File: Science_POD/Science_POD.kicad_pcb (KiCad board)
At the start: 2 copper layers, 24.6 x 59.9 mm, 10 parts, among them U1 Molex_SL_2, U2 AP1059, U3 ESP_8266_Breakout_Small, U4 Molex_SL_3, U5 Molex_SL_2

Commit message: finalised board
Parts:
- added G***: LOGO, MRDT_Silkscreens:Andrew_Van_Horn_Sig_15mm, B.Cu at (190.6, 106.8)
- added G***: LOGO, MRDT_Silkscreens:MRDT_Logo_10mm, B.Cu at (180.9, 110.9)
- added R2: 10K, Resistors_SMD:R_0603_HandSoldering, F.Cu at (176.0, 119.1)
- R1: value 100 -> 10K
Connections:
- U3 pad 7: /Ain -> Net-(R2-Pad2)
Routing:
- net /Ain: track 33.9 -> 30.3 mm
- net Net-(R2-Pad2): track 0.00 -> 3.13 mm
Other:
- board size 24.6 x 59.9 mm -> 25.9 x 59.9 mm
- board text added: "Moisture"
- board text added: "Sensor Pod, Rev 1 MRDT 2018 Missouri S&T Andrew Van Horn"
- board text added: "Temperature"

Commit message: Generated Final Gerbs
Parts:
- added D2: LED, Diodes_SMD:D_1206, F.Cu at (170.8, 93.4)
- added R3: 330, Resistors_SMD:R_0603_HandSoldering, F.Cu at (170.8, 98.3)
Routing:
- net /+3V3: track 36.6 -> 41.4 mm
- net Net-(D2-Pad2): track 0.00 -> 2.29 mm
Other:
- board size 25.9 x 59.9 mm -> 38.1 x 59.9 mm
- board text added: "Power"

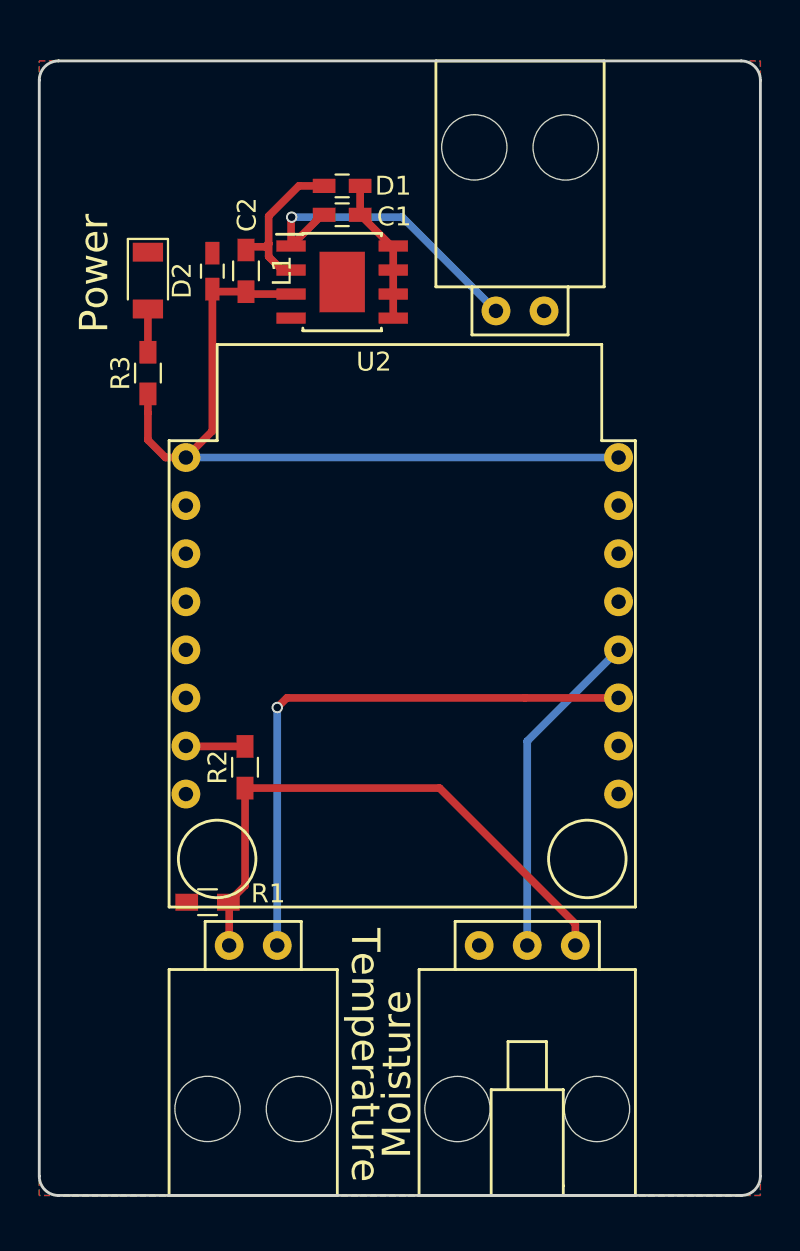
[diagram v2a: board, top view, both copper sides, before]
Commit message: Rev 2-added SL-3 for thermister. Fixed esp footprint
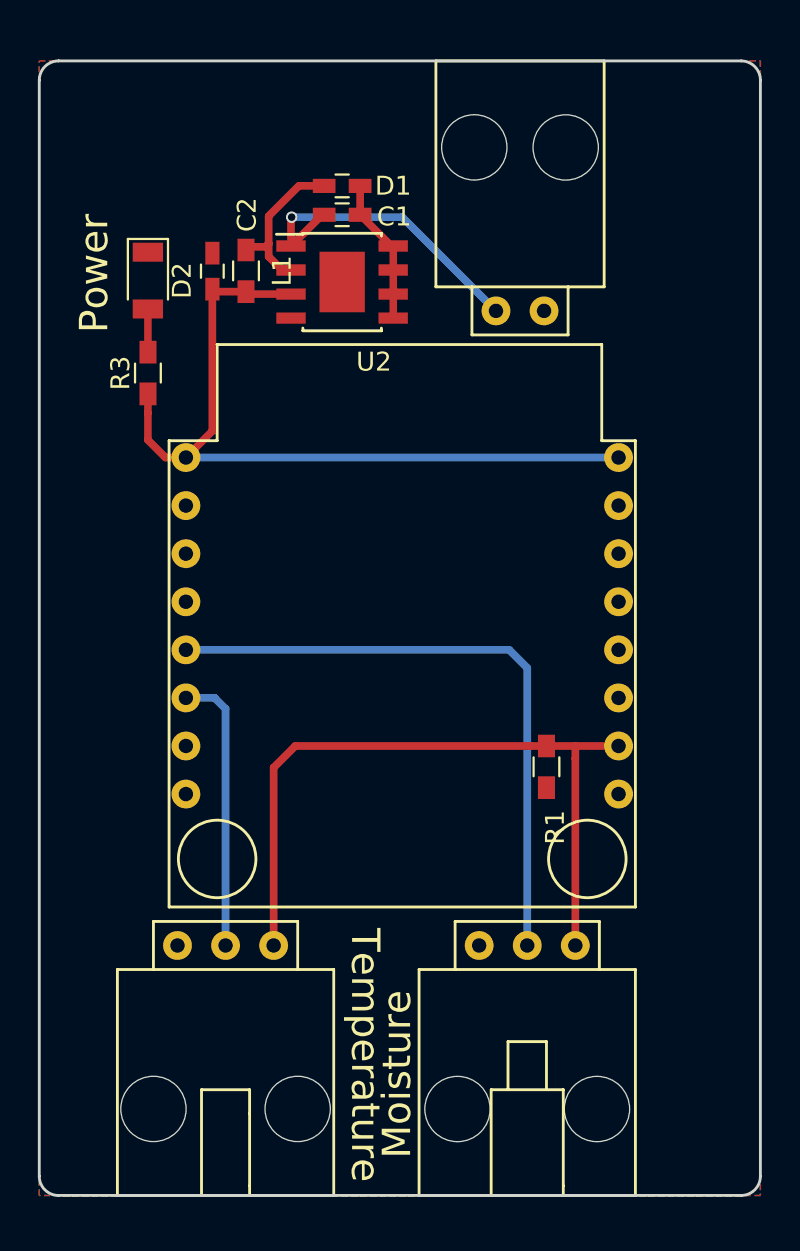
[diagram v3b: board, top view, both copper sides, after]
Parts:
- removed R2: 10K, Resistors_SMD:R_0603_HandSoldering
- U5: value Molex_SL_2 -> Molex_SL_3; footprint MRDT_Connectors:MOLEX_SL_2 -> MRDT_Connectors:MOLEX_SL_3_Horizontal
- moved R1 19.3 mm to (191.9, 119.1), turned to 90 degrees
- moved U5 1.46 mm to (174.9, 128.5)
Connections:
- R1 pad 1: /Ain -> /GND
- R1 pad 2: /GND -> /Ain
- U3 pad 10: /GND -> (no net)
- U3 pad 13: Net-(U3-Pad13) -> (no net)
- U3 pad 14: /D1 -> (no net)
- U3 pad 15: (no net) -> /Ain
- U3 pad 2: (no net) -> /GND
- U3 pad 5: (no net) -> /D2
- U3 pad 6: (no net) -> /D1
- U3 pad 7: Net-(R2-Pad2) -> (no net)
- U4 pad 2: Net-(U3-Pad13) -> /D2
- U5 pad 1: /D1 -> /Ain
- U5 pad 2: /Ain -> /D1
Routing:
- net /D2: track 0.00 -> 33.1 mm
- net Net-(U3-Pad13): track 17.6 -> 0.00 mm
- net /D1: track 30.8 -> 14.8 mm, vias 1 -> 0
- net /Ain: track 30.3 -> 38.6 mm
- net Net-(R2-Pad2): track 3.13 -> 0.00 mm
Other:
- board text added: "Sensor Pod, Rev 2 MRDT 2018 Missouri S&T Andrew Van Horn"
- board text removed: "Sensor Pod, Rev 1 MRDT 2018 Missouri S&T Andrew Van Horn"

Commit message: Generated Gerbs
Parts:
- moved G*** 19.8 mm to (180.1, 90.0)
- moved G*** 9.46 mm to (171.5, 109.8)
- moved U4 1.84 mm to (192.7, 128.5)
- moved U1 1.14 mm to (190.5, 93.9)
- moved C2 0.90 mm to (173.4, 93.0)
- moved U5 0.76 mm to (175.7, 128.5)
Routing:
- net /D2: track 33.1 -> 35.1 mm
- net Net-(C1-Pad1): track 16.8 -> 18.0 mm
- net /D1: track 14.8 -> 15.5 mm
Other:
- board text added: "+"
- board text added: "-"
- board text added: "Ain"
